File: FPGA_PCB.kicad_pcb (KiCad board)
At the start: 2 copper layers, 177.8 x 127 mm, 29 parts, among them J1 Conn_01x01_Male, J10 Conn_Coaxial, J11 Conn_Coaxial, J12 Conn_01x03_Male, J13 Conn_01x03_Male, J14 Conn_01x01_Male, J15 Conn_01x01_Male, J16 73096-2, J17 73096-2, J18 Conn_01x01_Male, J19 Conn_01x01_Male, J2 Conn_01x01_Male, J20 Conn_01x01_Male, J3 73096-2, J4 73096-2, J5 Conn_01x04_Male, J6 Conn_01x04_Male, J7 Conn_01x04_Male, J8 Conn_01x04_Male, J9 Conn_01x04_Male, SW1 SW_Push, U1 CPG08462

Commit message: ver 2.0
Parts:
- added C10: 100p, Capacitor_SMD:C_0805_2012Metric_Pad1.15x1.40mm_HandSolder, B.Cu at (103.5, 132.7)
- added C11: 100p, Capacitor_SMD:C_0805_2012Metric_Pad1.15x1.40mm_HandSolder, B.Cu at (133.3, 132.7)
- added C12: 100p, Capacitor_SMD:C_0805_2012Metric_Pad1.15x1.40mm_HandSolder, B.Cu at (103.5, 116.8)
- added C13: 100p, Capacitor_SMD:C_0805_2012Metric_Pad1.15x1.40mm_HandSolder, B.Cu at (133.3, 116.8)
- added C14: 100p, Capacitor_SMD:C_0805_2012Metric_Pad1.15x1.40mm_HandSolder, B.Cu at (103.5, 120.0)
- added C15: 100p, Capacitor_SMD:C_0805_2012Metric_Pad1.15x1.40mm_HandSolder, B.Cu at (133.3, 126.4)
- added C16: 100p, Capacitor_SMD:C_0805_2012Metric_Pad1.15x1.40mm_HandSolder, B.Cu at (103.5, 129.5)
- added C17: 100p, Capacitor_SMD:C_0805_2012Metric_Pad1.15x1.40mm_HandSolder, B.Cu at (172.1, 98.4)
- added C18: 100p, Capacitor_SMD:C_0805_2012Metric_Pad1.15x1.40mm_HandSolder, B.Cu at (172.1, 120.7)
- added C3: 100p, Capacitor_SMD:C_0805_2012Metric_Pad1.15x1.40mm_HandSolder, B.Cu at (133.3, 120.0)
- added C4: 100p, Capacitor_SMD:C_0805_2012Metric_Pad1.15x1.40mm_HandSolder, B.Cu at (103.5, 113.7)
- added C5: 100p, Capacitor_SMD:C_0805_2012Metric_Pad1.15x1.40mm_HandSolder, B.Cu at (133.3, 110.5)
- added C6: 100p, Capacitor_SMD:C_0805_2012Metric_Pad1.15x1.40mm_HandSolder, B.Cu at (103.5, 110.5)
- added C7: 100p, Capacitor_SMD:C_0805_2012Metric_Pad1.15x1.40mm_HandSolder, B.Cu at (133.3, 113.7)
- added C8: 100p, Capacitor_SMD:C_0805_2012Metric_Pad1.15x1.40mm_HandSolder, B.Cu at (103.5, 123.2)
- added C9: 100p, Capacitor_SMD:C_0805_2012Metric_Pad1.15x1.40mm_HandSolder, B.Cu at (133.3, 123.2)
- added J21: Conn_01x04_Male, Connector_PinHeader_2.54mm:PinHeader_1x04_P2.54mm_Vertical, F.Cu at (67.9, 93.3)
- added J22: Conn_01x04_Male, Connector_PinHeader_2.54mm:PinHeader_1x04_P2.54mm_Vertical, F.Cu at (67.9, 109.9)
- added J23: Conn_01x04_Male, Connector_PinHeader_2.54mm:PinHeader_1x04_P2.54mm_Vertical, F.Cu at (120.0, 140.3)
- added J24: Conn_01x01_Male, Connector_PinHeader_2.54mm:PinHeader_1x01_P2.54mm_Vertical, F.Cu at (179.7, 74.3)
- added J25: Conn_01x01_Male, Connector_PinHeader_2.54mm:PinHeader_1x01_P2.54mm_Vertical, F.Cu at (120.0, 31.8)
- added J26: Conn_01x03_Male, Connector_PinHeader_2.54mm:PinHeader_1x03_P2.54mm_Vertical, F.Cu at (160.0, 127.6)
- added J27: Conn_01x03_Male, Connector_PinHeader_2.54mm:PinHeader_1x03_P2.54mm_Vertical, F.Cu at (159.4, 87.0)
- added J28: Conn_Coaxial, Connector_Coaxial:BNC_TEConnectivity_1478204_Vertical, F.Cu at (192.4, 64.1)
- added JP1: Jumper_NC_Dual, Connector_PinHeader_2.54mm:PinHeader_1x03_P2.54mm_Vertical, F.Cu at (192.4, 87.0)
- added JP2: Jumper_NC_Dual, Connector_PinHeader_2.54mm:PinHeader_1x03_P2.54mm_Vertical, F.Cu at (192.4, 123.8)
- added U2: SN74LVC8T245DWR, SOIC127P1030X265-24N, F.Cu at (172.1, 99.1)
- added U3: SN74LVC8T245DWR, SOIC127P1030X265-24N, F.Cu at (172.1, 121.3)
- J16, J17: value 73096-2 -> Conn_01x04_Male; footprint 73096-2:73096-2 -> Connector_PinHeader_2.54mm:PinHeader_1x04_P2.54mm_Vertical
- J3, J4: value 73096-2 -> Conn_Coaxial; footprint 73096-2:73096-2 -> Connector_Coaxial:BNC_TEConnectivity_1478204_Vertical
- moved J15 175.2 mm to (192.4, 51.4)
- moved J16 78.4 mm to (95.9, 37.5), turned to 270 degrees
- moved J17 53.0 mm to (67.9, 76.8)
- moved C2 52.7 mm to (103.5, 126.4)
- moved J12 50.9 mm to (192.4, 116.2), turned to 180 degrees
- moved C1 43.6 mm to (133.3, 129.5)
- moved J18 41.8 mm to (170.2, 74.3)
- moved SW1 41.5 mm to (148.0, 48.9)
- moved R1 34.0 mm to (148.0, 42.5), turned to 180 degrees
- moved J10 29.6 mm to (156.2, 74.3)
- moved J6 28.9 mm to (75.6, 76.8)
- moved J7 28.9 mm to (75.6, 93.3)
- moved J8 28.9 mm to (75.6, 109.9)
- moved J5 28.9 mm to (95.9, 45.1)
- moved U1 28.9 mm to (101.0, 70.5)
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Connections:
- C2 pad 2: /VSSPST -> /VSS
- J12 pad 1: /clb_scan_in -> /clb_scan_in_3.3
- J12 pad 2: /clb_scan_out -> /clb_scan_out_3.3
- J12 pad 3: /clb_scan_en -> /clb_scan_en_3.3
- J13 pad 1: /conn_scan_in -> /conn_scan_in_3.3
- J13 pad 2: /conn_scan_out -> /conn_scan_out_3.3
- J13 pad 3: /conn_scan_en -> /conn_scan_en_3.3
- J15 pad 1: /VSSPST -> /3.3V
- J16 pad 1: /VDDPST -> /io[0]
- J16 pad 2: Net-(J16-Pad2) -> /io[1]
- J16 pad 3: Net-(J16-Pad3) -> /io[2]
- J16 pad 4: Net-(J16-Pad4) -> /io[3]
- J17 pad 1: /VSSPST -> /io[4]
- J17 pad 2: Net-(J17-Pad2) -> /io[5]
- J17 pad 3: Net-(J17-Pad3) -> /io[6]
- J17 pad 4: Net-(J17-Pad4) -> /io[7]
- J3 pad 2: Net-(J3-Pad2) -> /VSS
- J4 pad 1: /VSS -> /VDDPST
- J4 pad 2: Net-(J4-Pad2) -> /VSS
- U1 pad A6: /VSSPST -> /VSS
- U1 pad K8: /VSSPST -> /VSS
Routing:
- net /VSS: track 4.30 -> 121.9 mm, vias 1 -> 18
- net /3.3V: track 0.00 -> 58.7 mm, vias 0 -> 2
- net /clb_scan_en: track 32.3 -> 74.9 mm, vias 0 -> 2
- net /VDD: track 9.40 -> 48.8 mm, vias 0 -> 9
- net /clb_scan_in: track 37.4 -> 76.7 mm, vias 0 -> 2
- net /VDDPST: track 8.28 -> 47.0 mm, vias 0 -> 9
- net /conn_scan_out: track 41.2 -> 79.8 mm, vias 0 -> 1
- net /clb_scan_out: track 32.3 -> 67.1 mm, vias 0 -> 1
- net Net-(JP1-Pad2): track 0.00 -> 30.7 mm, vias 0 -> 1
- net /conn_scan_out_3.3: track 0.00 -> 27.5 mm, vias 0 -> 1
- net /clb_scan_in_3.3: track 0.00 -> 22.7 mm
- net Net-(JP2-Pad2): track 0.00 -> 21.1 mm
- net /clb_scan_en_3.3: track 0.00 -> 19.4 mm
- net /conn_scan_in: track 42.2 -> 61.3 mm, vias 0 -> 1
- net /VSSPST: track 18.6 -> 0.00 mm, vias 1 -> 0
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- added copper zone on In1.Cu, net /3.3V
- added copper zone on In1.Cu, net /VDD
- added copper zone on In1.Cu, net /VDDPST
- added copper zone on In2.Cu, net /VSS
- removed copper zone on F.Cu, net /VDD
- removed copper zone on F.Cu, net /VDDPST
- removed copper zone on B.Cu, net /VSS
- removed copper zone on B.Cu, net /VSSPST
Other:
- copper layers 2 -> 4
- board text added: "0"
- board text added: "1"
- board text added: "10"
- board text added: "11"
- board text added: "12"
- board text added: "13"
- board text added: "14"
- board text added: "15"
- board text added: "16"
- board text added: "17"
- board text added: "18"
- board text added: "19"
- board text added: "2"
- board text added: "3"
- board text added: "3.3V"
- board text added: "4"
- board text added: "5"
- board text added: "6"
- board text added: "7"
- board text added: "8"
- board text added: "9"
- board text added: "CLK"
- board text added: "OFF"
- board text added: "ON"
- board text added: "RESET"
- board text added: "SCAN_CLK"
- board text added: "To use 1.8V input, turn level shifters off"
- board text added: "VDD"
- board text added: "VDDPST"
- board text added: "VSS_backup"
- board text added: "clb_scan: 1.8V"
- board text added: "clb_scan: 3.3V"
- board text added: "conn_scan: 1.8V"
- board text added: "conn_scan: 3.3V"
- board text added: "en"
- board text added: "in"
- board text added: "out"

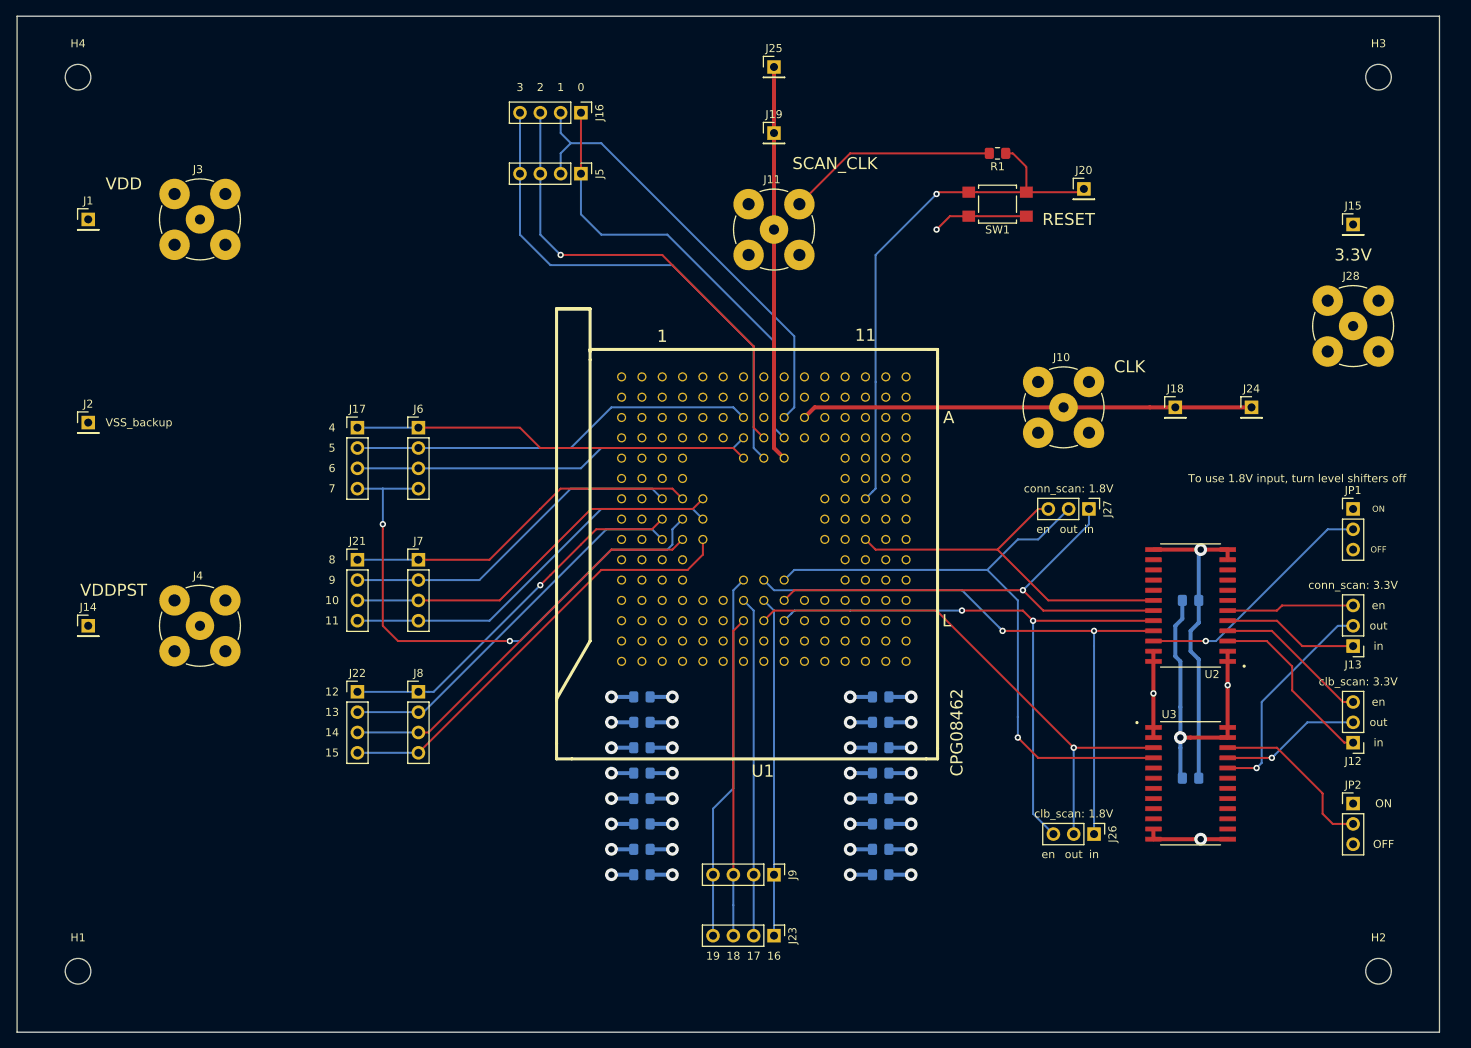
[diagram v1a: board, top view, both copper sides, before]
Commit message: ver 3.0: added i/o level shifters
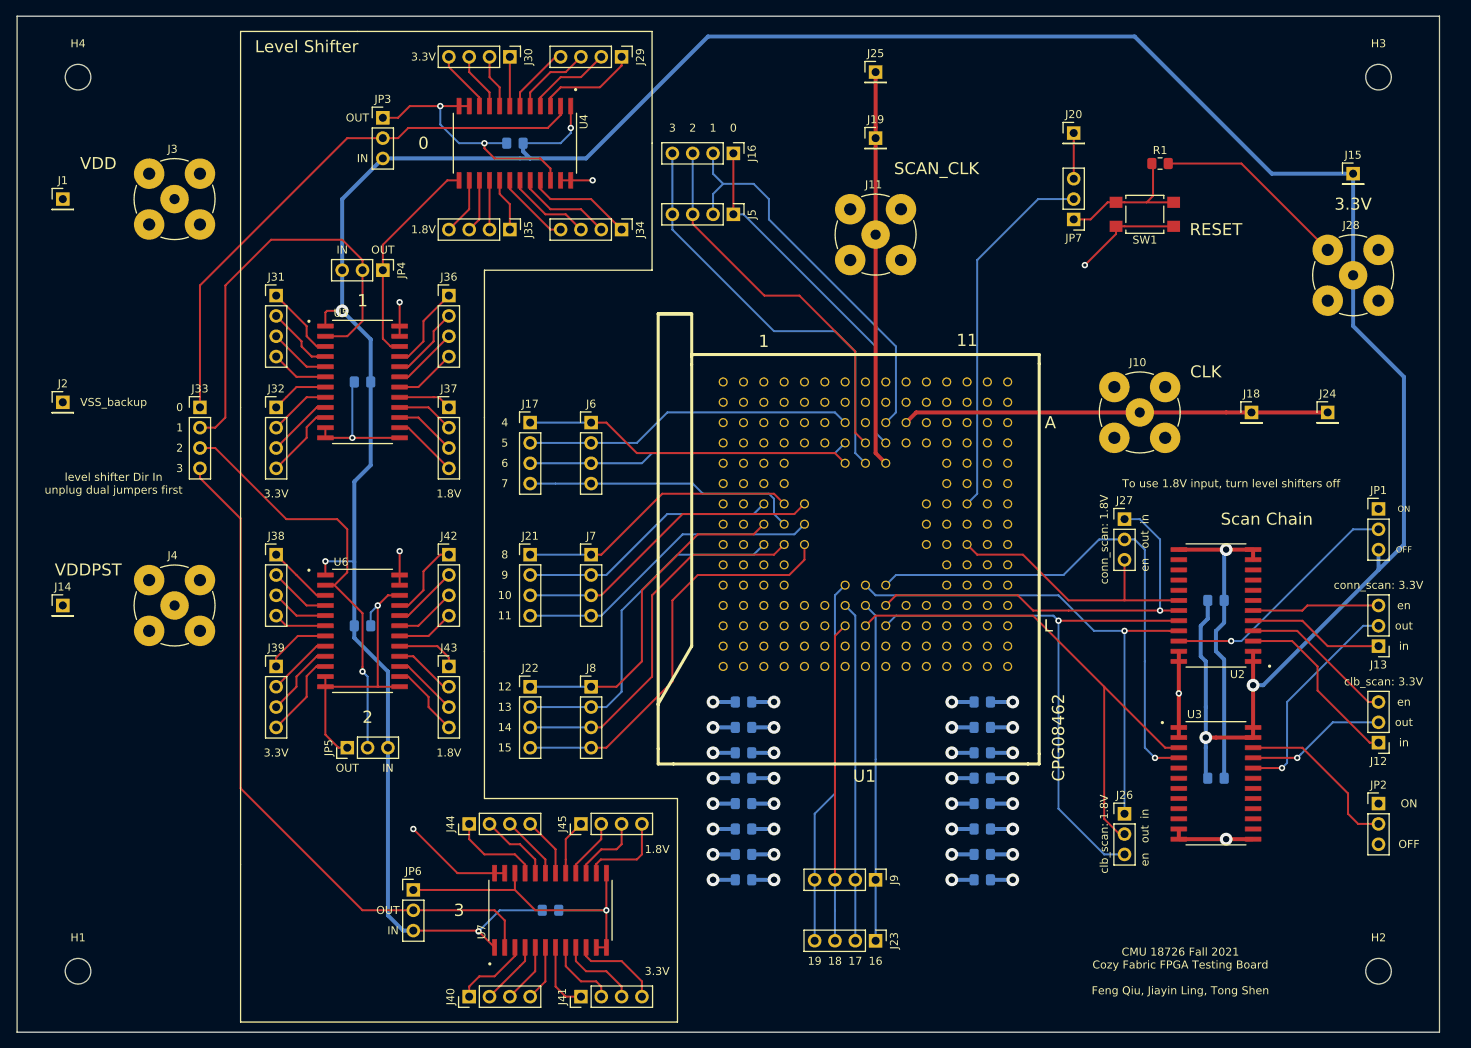
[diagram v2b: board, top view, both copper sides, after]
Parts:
- added C19: 100p, Capacitor_SMD:C_0805_2012Metric_Pad1.15x1.40mm_HandSolder, B.Cu at (92.1, 137.2)
- added C20: 100p, Capacitor_SMD:C_0805_2012Metric_Pad1.15x1.40mm_HandSolder, B.Cu at (87.6, 41.3)
- added C21: 100p, Capacitor_SMD:C_0805_2012Metric_Pad1.15x1.40mm_HandSolder, B.Cu at (68.6, 101.6)
- added C22: 100p, Capacitor_SMD:C_0805_2012Metric_Pad1.15x1.40mm_HandSolder, B.Cu at (68.6, 71.1)
- added J29: Conn_01x04_Male, Connector_PinHeader_2.54mm:PinHeader_1x04_P2.54mm_Vertical, F.Cu at (101.0, 30.5)
- added J30: Conn_01x04_Male, Connector_PinHeader_2.54mm:PinHeader_1x04_P2.54mm_Vertical, F.Cu at (87.0, 30.5)
- added J31: Conn_01x04_Male, Connector_PinHeader_2.54mm:PinHeader_1x04_P2.54mm_Vertical, F.Cu at (57.8, 60.3)
- added J32: Conn_01x04_Male, Connector_PinHeader_2.54mm:PinHeader_1x04_P2.54mm_Vertical, F.Cu at (57.8, 74.3)
- added J33: Conn_01x04_Male, Connector_PinHeader_2.54mm:PinHeader_1x04_P2.54mm_Vertical, F.Cu at (48.3, 74.3)
- added J34: Conn_01x04_Male, Connector_PinHeader_2.54mm:PinHeader_1x04_P2.54mm_Vertical, F.Cu at (101.0, 52.1)
- added J35: Conn_01x04_Male, Connector_PinHeader_2.54mm:PinHeader_1x04_P2.54mm_Vertical, F.Cu at (87.0, 52.1)
- added J36: Conn_01x04_Male, Connector_PinHeader_2.54mm:PinHeader_1x04_P2.54mm_Vertical, F.Cu at (79.4, 60.3)
- added J37: Conn_01x04_Male, Connector_PinHeader_2.54mm:PinHeader_1x04_P2.54mm_Vertical, F.Cu at (79.4, 74.3)
- added J38: Conn_01x04_Male, Connector_PinHeader_2.54mm:PinHeader_1x04_P2.54mm_Vertical, F.Cu at (57.8, 92.7)
- added J39: Conn_01x04_Male, Connector_PinHeader_2.54mm:PinHeader_1x04_P2.54mm_Vertical, F.Cu at (57.8, 106.7)
- added J40: Conn_01x04_Male, Connector_PinHeader_2.54mm:PinHeader_1x04_P2.54mm_Vertical, F.Cu at (81.9, 148.0)
- added J41: Conn_01x04_Male, Connector_PinHeader_2.54mm:PinHeader_1x04_P2.54mm_Vertical, F.Cu at (95.9, 148.0)
- added J42: Conn_01x04_Male, Connector_PinHeader_2.54mm:PinHeader_1x04_P2.54mm_Vertical, F.Cu at (79.4, 92.7)
- added J43: Conn_01x04_Male, Connector_PinHeader_2.54mm:PinHeader_1x04_P2.54mm_Vertical, F.Cu at (79.4, 106.7)
- added J44: Conn_01x04_Male, Connector_PinHeader_2.54mm:PinHeader_1x04_P2.54mm_Vertical, F.Cu at (81.9, 126.4)
- added J45: Conn_01x04_Male, Connector_PinHeader_2.54mm:PinHeader_1x04_P2.54mm_Vertical, F.Cu at (95.9, 126.4)
- added JP3: Jumper_NC_Dual, Connector_PinHeader_2.54mm:PinHeader_1x03_P2.54mm_Vertical, F.Cu at (71.1, 38.1)
- added JP4: Jumper_NC_Dual, Connector_PinHeader_2.54mm:PinHeader_1x03_P2.54mm_Vertical, F.Cu at (71.1, 57.1)
- added JP5: Jumper_NC_Dual, Connector_PinHeader_2.54mm:PinHeader_1x03_P2.54mm_Vertical, F.Cu at (66.7, 116.8)
- added JP6: Jumper_NC_Dual, Connector_PinHeader_2.54mm:PinHeader_1x03_P2.54mm_Vertical, F.Cu at (74.9, 134.6)
- added JP7: Jumper_NC_Dual, Connector_PinHeader_2.54mm:PinHeader_1x03_P2.54mm_Vertical, F.Cu at (157.5, 50.8)
- added U4: SN74LVC8T245DWR, SOIC127P1030X265-24N, F.Cu at (87.6, 41.3)
- added U5: SN74LVC8T245DWR, SOIC127P1030X265-24N, F.Cu at (68.6, 71.1)
- added U6: SN74LVC8T245DWR, SOIC127P1030X265-24N, F.Cu at (68.6, 102.2)
- added U7: SN74LVC8T245DWR, SOIC127P1030X265-24N, F.Cu at (92.1, 137.2)
- moved J17 21.6 mm to (89.5, 76.2)
- moved J21 21.6 mm to (89.5, 92.7)
- moved J22 21.6 mm to (89.5, 109.2)
- moved J6 21.6 mm to (97.2, 76.2)
- moved J7 21.6 mm to (97.2, 92.7)
- moved J8 21.6 mm to (97.2, 109.2)
- moved R1 20.4 mm to (168.3, 43.8), turned to 0 degrees
- moved J16 19.7 mm to (114.9, 42.5)
- moved J5 19.7 mm to (114.9, 50.2)
- moved SW1 18.5 mm to (166.4, 50.2)
- moved C1 12.7 mm to (146.1, 130.2)
- moved C11 12.7 mm to (146.1, 133.3)
- moved C13 12.7 mm to (146.1, 117.5)
- moved C15 12.7 mm to (146.1, 127.0)
- moved C3 12.7 mm to (146.1, 120.7)
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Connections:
- J20 pad 1: /RST -> /RST_header
- R1 pad 1: /RST -> /RST_switch
- SW1 pad 2: /RST -> /RST_switch
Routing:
- net /3.3V: track 58.7 -> 398.2 mm, vias 2 -> 6
- net /VSS: track 121.9 -> 279.1 mm, vias 18 -> 23
- net /IOLeverShifter/dir3: track 0.00 -> 85.3 mm
- net /IOLeverShifter/dir0: track 0.00 -> 70.3 mm
- net /IOLeverShifter/dir1: track 0.00 -> 53.8 mm
- net /IOLeverShifter/dir2: track 0.00 -> 53.4 mm, vias 0 -> 1
- net /io[7]: track 70.4 -> 35.0 mm, vias 2 -> 0
- net /VDDPST: track 47.0 -> 72.6 mm, vias 9 -> 13
- net /RST: track 66.9 -> 46.2 mm, vias 1 -> 0
- net /RST_switch: track 0.00 -> 18.6 mm
- net /conn_scan_out: track 79.8 -> 64.8 mm
- net /IOLeverShifter/b[0]: track 0.00 -> 13.3 mm
- net /io[5]: track 54.7 -> 41.5 mm
- net /conn_scan_en: track 47.6 -> 34.4 mm
- net /IOLeverShifter/a[0]: track 0.00 -> 12.7 mm
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- removed copper zone on In1.Cu, net /3.3V
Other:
- board text added: "1.8V"
- board text added: "CMU 18726 Fall 2021 Cozy Fabric FPGA Testing Board Feng Qiu, Jiayin Ling, Tong Shen"
- board text added: "IN"
- board text added: "Level Shifter"
- board text added: "OUT"
- board text added: "Scan Chain"
- board text added: "level shifter Dir In unplug dual jumpers first"

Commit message: ver 4.0: added 1.8V pin
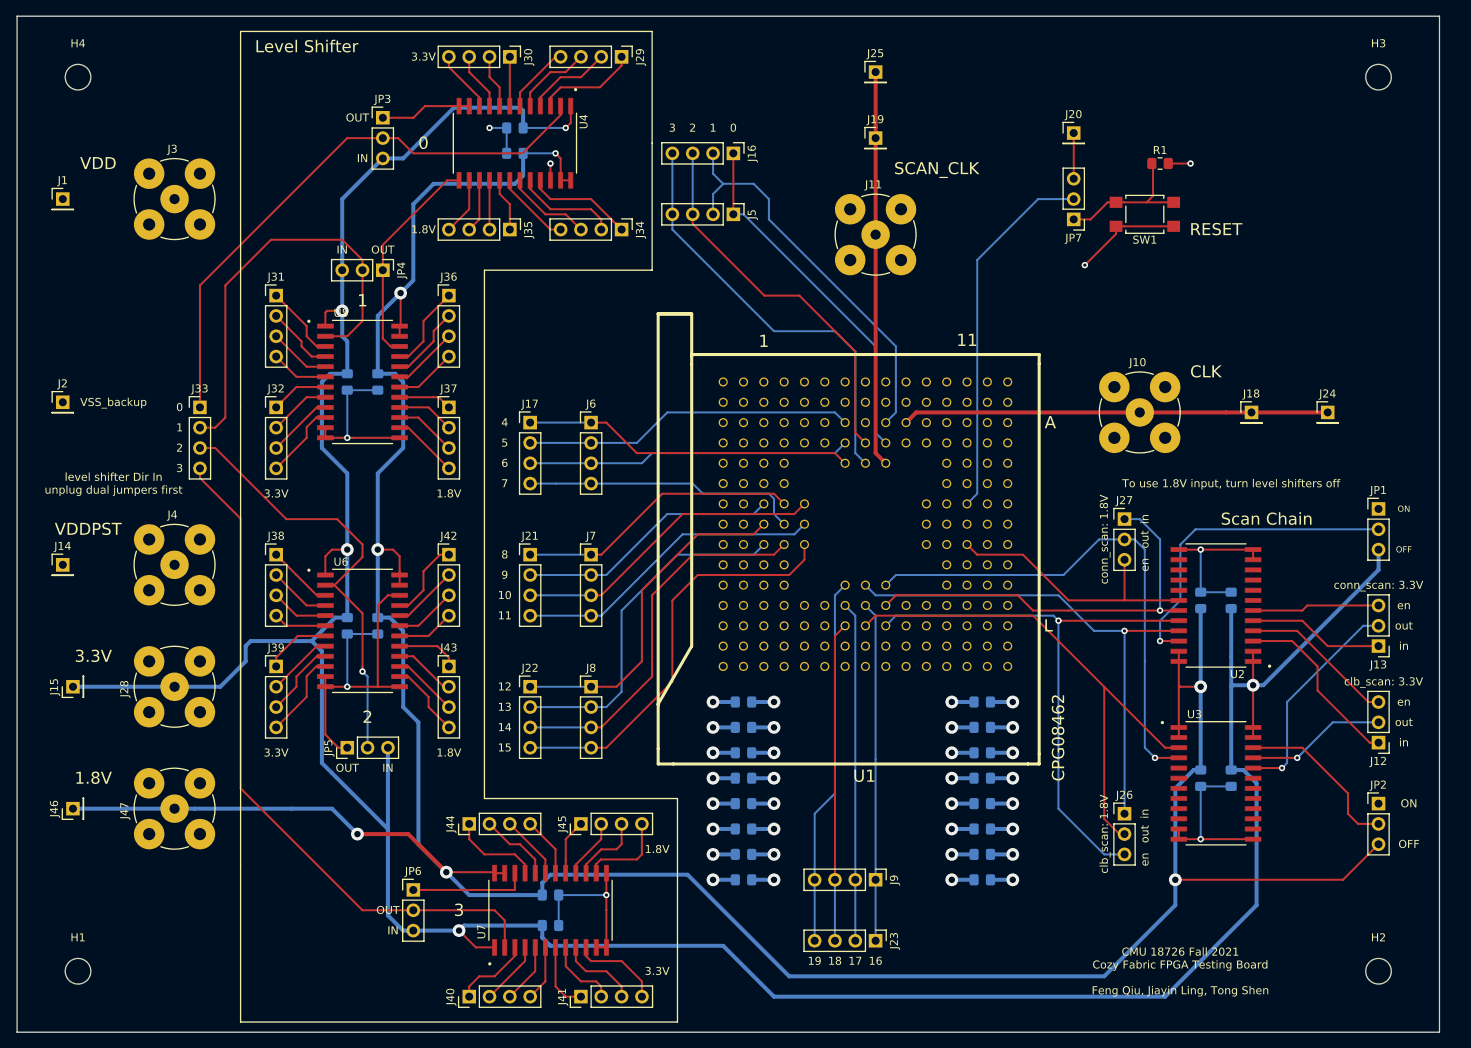
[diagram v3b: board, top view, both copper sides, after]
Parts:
- added C23: 100p, Capacitor_SMD:C_0805_2012Metric_Pad1.15x1.40mm_HandSolder, B.Cu at (70.5, 101.6)
- added C24: 100p, Capacitor_SMD:C_0805_2012Metric_Pad1.15x1.40mm_HandSolder, B.Cu at (70.5, 71.1)
- added C25: 100p, Capacitor_SMD:C_0805_2012Metric_Pad1.15x1.40mm_HandSolder, B.Cu at (173.4, 98.4)
- added C26: 100p, Capacitor_SMD:C_0805_2012Metric_Pad1.15x1.40mm_HandSolder, B.Cu at (173.4, 120.7)
- added C27: 100p, Capacitor_SMD:C_0805_2012Metric_Pad1.15x1.40mm_HandSolder, B.Cu at (87.6, 42.5)
- added C28: 100p, Capacitor_SMD:C_0805_2012Metric_Pad1.15x1.40mm_HandSolder, B.Cu at (92.1, 135.3)
- added J46: Conn_01x01_Male, Connector_PinHeader_2.54mm:PinHeader_1x01_P2.54mm_Vertical, F.Cu at (32.4, 124.5)
- added J47: Conn_Coaxial, Connector_Coaxial:BNC_TEConnectivity_1478204_Vertical, F.Cu at (45.1, 124.5)
- moved J15 172.4 mm to (32.4, 109.2), turned to 90 degrees
- moved J28 156.0 mm to (45.1, 109.2), turned to 90 degrees
- moved J14 5.08 mm to (31.1, 94.0)
- moved J4 5.08 mm to (45.1, 94.0)
- moved C17 1.91 mm to (177.2, 98.4), turned to 90 degrees
- moved C18 1.91 mm to (177.2, 120.7), turned to 270 degrees
- moved C19 1.91 mm to (92.1, 139.1)
- moved C20 1.91 mm to (87.6, 39.4)
- moved C21 1.91 mm to (66.7, 101.6), turned to 270 degrees
- moved C22 1.91 mm to (66.7, 71.1), turned to 270 degrees
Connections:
- JP2 pad 3: /VDDPST -> /1.8V
- U2 pad 23: /VDDPST -> /1.8V
- U2 pad 24: /VDDPST -> /1.8V
- U3 pad 1: /VDDPST -> /1.8V
- U3 pad 2: /VDDPST -> /1.8V
- U4 pad 23: /VDDPST -> /1.8V
- U4 pad 24: /VDDPST -> /1.8V
- U5 pad 23: /VDDPST -> /1.8V
- U5 pad 24: /VDDPST -> /1.8V
- U6 pad 23: /VDDPST -> /1.8V
- U6 pad 24: /VDDPST -> /1.8V
- U7 pad 23: /VDDPST -> /1.8V
- U7 pad 24: /VDDPST -> /1.8V
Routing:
- net /1.8V: track 0.00 -> 373.5 mm, vias 0 -> 7
- net /VSS: track 279.1 -> 233.5 mm, vias 23 -> 24
- net /VDDPST: track 72.6 -> 35.6 mm, vias 13 -> 8
- net Net-(JP1-Pad2): track 30.7 -> 41.0 mm
- net /3.3V: track 398.2 -> 392.5 mm, vias 6 -> 5
- net /IOLeverShifter/dir2: track 53.4 -> 55.0 mm
- net /IOLeverShifter/dir0: track 70.3 -> 71.9 mm
- net /IOLeverShifter/b[1]: track 12.1 -> 12.8 mm
